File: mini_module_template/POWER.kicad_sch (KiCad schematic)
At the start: 15 parts, among them J2 PASS THROUYH BUS CONENCTOR, J4 PASS THROUYH BUS CONENCTOR, U5 AZ1117-3.3

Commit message: Leyout rev 1
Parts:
- removed C20: 10u, Capacitor_SMD:C_0805_2012Metric, symbol Device:C
- removed D6: HV_PWR, Diode_SMD:D_0603_1608Metric, symbol Device:LED
- removed J2, J4: PASS THROUYH BUS CONENCTOR, symbol Connector_Generic:Conn_01x07
- added C25, C26: 10u, Capacitor_SMD:C_1206_3216Metric, symbol Device:C
- added C28, C29: 22u, Capacitor_SMD:C_1206_3216Metric, symbol Device:C
- added C30: 100n, Capacitor_SMD:C_0603_1608Metric, symbol Device:C
- added C31: 1n, Capacitor_SMD:C_0603_1608Metric, symbol Device:C
- added C32: 100n, Capacitor_SMD:C_0402_1005Metric, symbol Device:C
- added J2, J3: ~, parts:DSUB-7w2, symbol DSUB_7w2:DSUB-7w2
- added L1: 3.3u, Inductor_SMD:L_Changjiang_FNR4030S, symbol Device:L
- added R25: 54k9, Resistor_SMD:R_0402_1005Metric, symbol Device:R
- added R26: 10k, Resistor_SMD:R_0402_1005Metric, symbol Device:R
- added U5: TPS563200, Package_TO_SOT_SMD:SOT-23-6, symbol Regulator_Switching:TPS563200
- C20: renamed from C15; footprint Capacitor_SMD:C_1206_3216Metric -> Capacitor_SMD:C_0805_2012Metric
- renumbered C16 to C21, C17 to C22, C18 to C23, C19 to C24, R22 to R27, R25 to R29, R23 to R30, U5 to U4
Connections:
- net +12V: now also C25.1, C26.1, J2.2 (D11), J3.2 (D11), U5.3 (VIN)
- net +5V: now also C28.1, C29.1, C30.1, C31.1, C32.1, L1.2, R25.1
- net CAN_H: now also J2.3 (D12), J3.3 (D12)
- net CAN_L: now also J2.4 (D13), J3.4 (D13)
- net GND: now also R24.2, C25.2, C26.2, C28.2, C29.2, C30.2, C31.2, J2.5 (D21), J2.7 (H2), J3.5 (D21), J3.7 (H2), R26.2, U5.1 (GND)
- net VCC: now also J2.1 (H1), J3.1 (H1); no longer R24.1
- new net: C32.2, U5.6 (VBST)
- new net: L1.1, U5.2 (SW)
- new net: R24.1, U5.5 (EN)
- new net: R25.2, R26.1, U5.4 (VFB)
- new net NC: J2.6 (D22), J3.6 (D22)
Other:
- note added: "DC-DC 12V TO 5V"
- note added: "Vout= 0.768(1+R1/R2) Vout=5V R1=54k9 R2=10k Vout=>4.984V"
- note removed: "SOME 12V TO 5V"

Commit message: a
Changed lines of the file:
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@@
-	)
-	(junction
-		(at 212.09 39.37)
-		(diameter 0)
-		(color 0 0 0 0)
 	)
 	(junction
@@
 		)
 		(stroke
-			(width 0)
-			(type default)
-		)
-	)
-	(wire
-		(pts
-			(xy 212.09 39.37) (xy 212.09 40.64)
-		)
-		(stroke

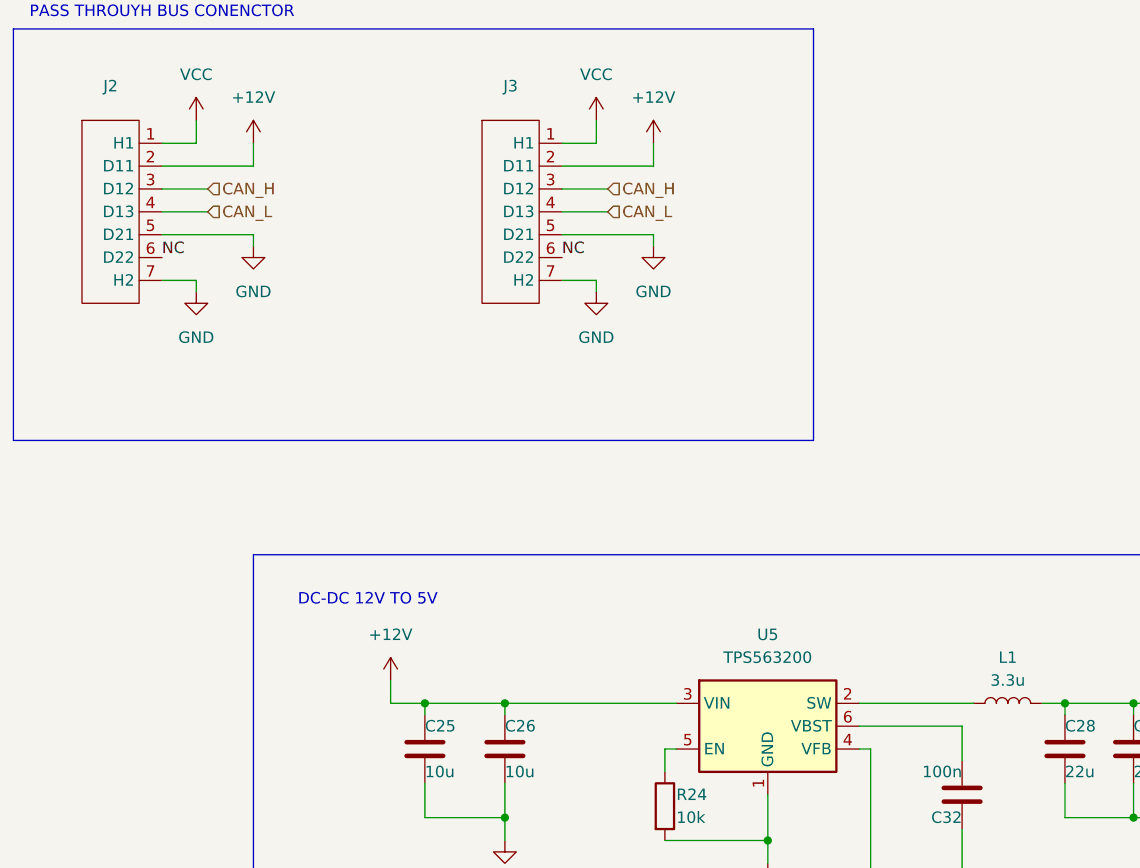
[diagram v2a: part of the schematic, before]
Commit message: fixed can and usb traces
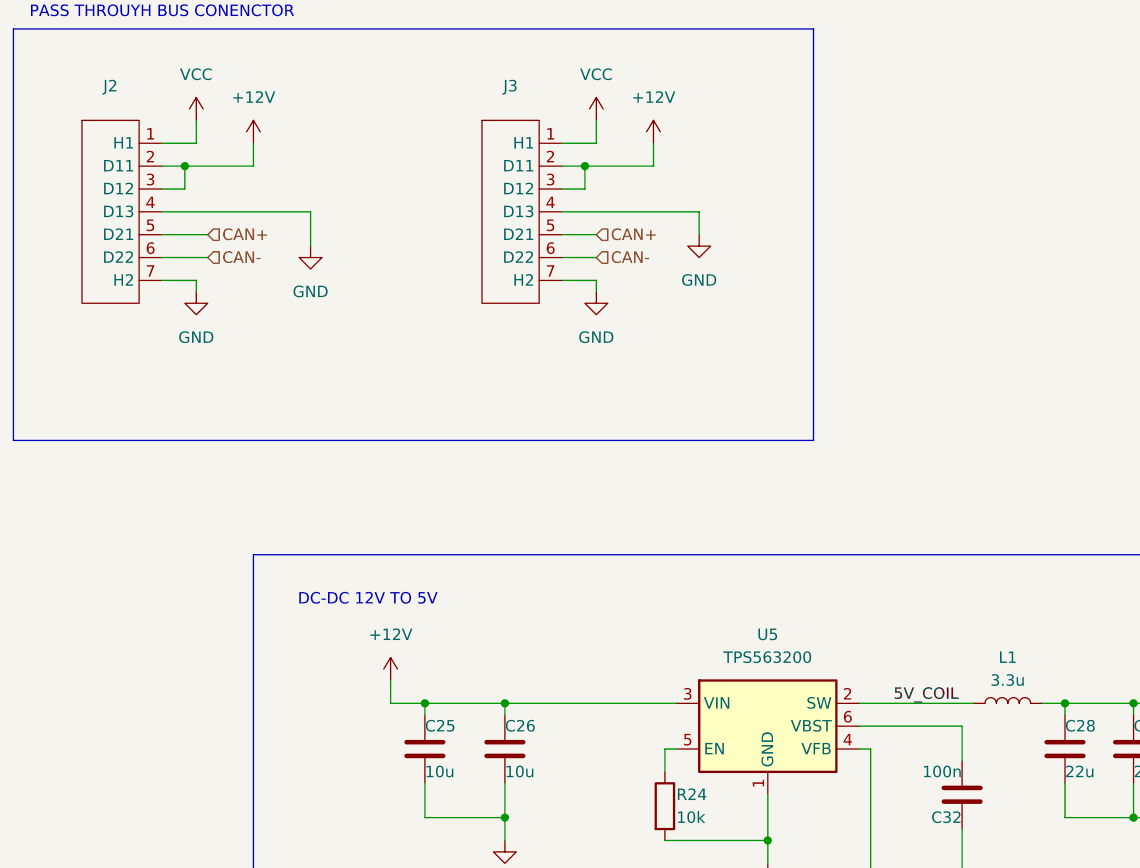
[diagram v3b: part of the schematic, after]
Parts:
- C25, C26, C28, C29: footprint Capacitor_SMD:C_1206_3216Metric -> Capacitor_SMD:C_0805_2012Metric
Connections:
- net CAN_H is gone; now on net +12V: J2.3 (D12), J3.3 (D12)
- net CAN_L is gone; now on net GND: J2.4 (D13), J3.4 (D13)
- net GND: no longer J2.5 (D21), J3.5 (D21)
- net 5V_COIL: now reaches L1.1, U5.2 (SW)
- net NC renamed CAN-
- new net CAN+: J2.5 (D21), J3.5 (D21)
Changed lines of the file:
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@@
 	)
 	(junction
+		(at 87.63 34.29)
+		(diameter 0)
+		(color 0 0 0 0)
+	)
+	(junction
 		(at 140.97 93.98)
 		(diameter 0)
@@
 	)
 	(junction
+		(at 43.18 34.29)
+		(diameter 0)
+		(color 0 0 0 0)
+	)
+	(junction
 		(at 171.45 93.98)
 		(diameter 0)
@@
 	(wire
 		(pts
-			(xy 50.8 41.91) (xy 40.64 41.91)
+			(xy 107.95 104.14) (xy 107.95 109.22)
 		)
 		(stroke
@@
 	(wire
 		(pts
-			(xy 107.95 104.14) (xy 107.95 109.22)
+			(xy 57.15 43.18) (xy 57.15 39.37)
 		)
 		(stroke
@@
 	(wire
 		(pts
+			(xy 87.63 34.29) (xy 95.25 34.29)
+		)
+		(stroke
+			(width 0)
+			(type default)
+		)
+	)
+	(wire
+		(pts
+			(xy 40.64 39.37) (xy 57.15 39.37)
+		)
+		(stroke
+			(width 0)
+			(type default)
+		)
+	)
+	(wire
+		(pts
 			(xy 44.45 29.21) (xy 44.45 31.75)
 		)
@@
 	(wire
 		(pts
+			(xy 85.09 41.91) (xy 88.9 41.91)
+		)
+		(stroke
+			(width 0)
+			(type default)
+		)
+	)
+	(wire
+		(pts
 			(xy 129.54 107.95) (xy 129.54 113.03)
 		)
@@
 	(wire
 		(pts
-			(xy 95.25 41.91) (xy 85.09 41.91)
-		)
-		(stroke
-			(width 0)
-			(type default)
-		)
-	)
-	(wire
-		(pts
 			(xy 189.23 59.69) (xy 196.85 59.69)
 		)
@@
 	(wire
 		(pts
+			(xy 100.33 39.37) (xy 85.09 39.37)
+		)
+		(stroke
+			(width 0)
+			(type default)
+		)
+	)
+	(wire
+		(pts
 			(xy 163.83 93.98) (xy 171.45 93.98)
 		)
@@
 	(wire
 		(pts
-			(xy 85.09 36.83) (xy 90.17 36.83)
+			(xy 85.09 36.83) (xy 87.63 36.83)
 		)
 		(stroke
@@
 	(wire
 		(pts
+			(xy 40.64 36.83) (xy 43.18 36.83)
+		)
+		(stroke
+			(width 0)
+			(type default)
+		)
+	)
+	(wire
+		(pts
 			(xy 176.53 93.98) (xy 176.53 104.14)
 		)
@@
 	(wire
 		(pts
+			(xy 40.64 44.45) (xy 45.72 44.45)
+		)
+		(stroke
+			(width 0)
+			(type default)
+		)
+	)
+	(wire
+		(pts
 			(xy 129.54 100.33) (xy 129.54 96.52)
 		)
@@
 	(wire
 		(pts
-			(xy 204.47 48.26) (xy 204.47 59.69)
+			(xy 40.64 41.91) (xy 45.72 41.91)
 		)
 		(stroke
@@
 	(wire
 		(pts
-			(xy 40.64 39.37) (xy 45.72 39.37)
+			(xy 85.09 44.45) (xy 88.9 44.45)
 		)
 		(stroke
@@
 	(wire
 		(pts
-			(xy 95.25 43.18) (xy 95.25 41.91)
+			(xy 204.47 48.26) (xy 204.47 59.69)
+		)
+		(stroke
+			(width 0)
+			(type default)
+		)
+	)
+	(wire
+		(pts
+			(xy 87.63 34.29) (xy 87.63 36.83)
 		)
 		(stroke
@@
 	(wire
 		(pts
-			(xy 50.8 43.18) (xy 50.8 41.91)
+			(xy 43.18 34.29) (xy 43.18 36.83)
 		)
 		(stroke
@@
 	(wire
 		(pts
-			(xy 50.8 34.29) (xy 40.64 34.29)
+			(xy 50.8 34.29) (xy 43.18 34.29)
 		)
 		(stroke
@@
 	(wire
 		(pts
+			(xy 87.63 34.29) (xy 85.09 34.29)
+		)
+		(stroke
+			(width 0)
+			(type default)
+		)
+	)
+	(wire
+		(pts
 			(xy 41.91 170.18) (xy 41.91 171.45)
 		)
@@
 	(wire
 		(pts
-			(xy 85.09 39.37) (xy 90.17 39.37)
+			(xy 189.23 39.37) (xy 196.85 39.37)
 		)
 		(stroke
@@
 	(wire
 		(pts
-			(xy 189.23 39.37) (xy 196.85 39.37)
+			(xy 100.33 41.91) (xy 100.33 39.37)
 		)
 		(stroke
@@
 	(wire
 		(pts
-			(xy 95.25 34.29) (xy 85.09 34.29)
+			(xy 43.18 34.29) (xy 40.64 34.29)
 		)
 		(stroke
@@
 	(wire
 		(pts
-			(xy 40.64 36.83) (xy 45.72 36.83)
-		)
-		(stroke
-			(width 0)
-			(type default)
-		)
-	)
-	(wire
-		(pts
 			(xy 160.02 39.37) (xy 160.02 40.64)
 		)
@@
 		)
 	)
-	(label "NC"
-		(at 40.64 44.45 0)
-		(fields_autoplaced yes)
-		(effects
-			(font
-				(size 1.27 1.27)
-			)
-			(justify left bottom)
-		)
-	)
-	(label "NC"
-		(at 85.09 44.45 0)
+	(label "5V_COIL"
+		(at 121.92 93.98 0)
 		(fields_autoplaced yes)
 		(effects
@@
 		)
 	)
-	(hierarchical_label "CAN_L"
+	(hierarchical_label "CAN-"
 		(shape input)
-		(at 45.72 39.37 0)
+		(at 45.72 44.45 0)
 		(fields_autoplaced yes)
 		(effects
@@
 		)
 	)
-	(hierarchical_label "CAN_L"
+	(hierarchical_label "CAN-"
 		(shape input)
-		(at 90.17 39.37 0)
+		(at 88.9 44.45 0)
 		(fields_autoplaced yes)
 		(effects
@@
 		)
 	)
-	(hierarchical_label "CAN_H"
+	(hierarchical_label "CAN+"
 		(shape input)
-		(at 90.17 36.83 0)
+		(at 88.9 41.91 0)
 		(fields_autoplaced yes)
 		(effects
@@
 		)
 	)
-	(hierarchical_label "CAN_H"
-		(shape input)
-		(at 45.72 36.83 0)
+	(hierarchical_label "V_SENSE"
+		(shape output)
+		(at 44.45 170.18 0)
 		(fields_autoplaced yes)
 		(effects
@@
 		)
 	)
-	(hierarchical_label "V_SENSE"
-		(shape output)
-		(at 44.45 170.18 0)
+	(hierarchical_label "CAN+"
+		(shape input)
+		(at 45.72 41.91 0)
 		(fields_autoplaced yes)
 		(effects
@@
 			)
 		)
-		(property "Footprint" "Capacitor_SMD:C_1206_3216Metric"
+		(property "Footprint" "Capacitor_SMD:C_0805_2012Metric"
 			(at 149.5552 102.87 0)
 			(effects
@@
 			)
 		)
-		(property "Footprint" "Capacitor_SMD:C_1206_3216Metric"
+		(property "Footprint" "Capacitor_SMD:C_0805_2012Metric"
 			(at 141.9352 102.87 0)
 			(effects
@@
 	(symbol
 		(lib_id "power:GND")
-		(at 95.25 43.18 0)
+		(at 100.33 41.91 0)
 		(unit 1)
 		(exclude_from_sim no)
@@
 		(fields_autoplaced yes)
 		(property "Reference" "#PWR050"
-			(at 95.25 49.53 0)
+			(at 100.33 48.26 0)
 			(effects
 				(font
@@
 		)
 		(property "Value" "GND"
-			(at 95.25 48.26 0)
+			(at 100.33 46.99 0)
 			(effects
 				(font
@@
 		)
 		(property "Footprint" ""
-			(at 95.25 43.18 0)
+			(at 100.33 41.91 0)
 			(effects
 				(font
@@
 		)
 		(property "Datasheet" ""
-			(at 95.25 43.18 0)
+			(at 100.33 41.91 0)
 			(effects
 				(font
@@
 		)
 		(property "Description" "Power symbol creates a global label with name \"GND\" , ground"
-			(at 95.25 43.18 0)
+			(at 100.33 41.91 0)
 			(effects
 				(font
@@
 			)
 		)
-		(property "Footprint" "Capacitor_SMD:C_1206_3216Metric"
+		(property "Footprint" "Capacitor_SMD:C_0805_2012Metric"
 			(at 79.7052 102.87 0)
 			(effects
@@
 	(symbol
 		(lib_id "power:GND")
-		(at 50.8 43.18 0)
+		(at 57.15 43.18 0)
 		(unit 1)
 		(exclude_from_sim no)
@@
 		(fields_autoplaced yes)
 		(property "Reference" "#PWR049"
-			(at 50.8 49.53 0)
+			(at 57.15 49.53 0)
 			(effects
 				(font
@@
 		)
 		(property "Value" "GND"
-			(at 50.8 48.26 0)
+			(at 57.15 48.26 0)
 			(effects
 				(font
@@
 		)
 		(property "Footprint" ""
-			(at 50.8 43.18 0)
+			(at 57.15 43.18 0)
 			(effects
 				(font
@@
 		)
 		(property "Datasheet" ""
-			(at 50.8 43.18 0)
+			(at 57.15 43.18 0)
 			(effects
 				(font
@@
 		)
 		(property "Description" "Power symbol creates a global label with name \"GND\" , ground"
-			(at 50.8 43.18 0)
+			(at 57.15 43.18 0)
 			(effects
 				(font
@@
 			)
 		)
-		(property "Footprint" "Capacitor_SMD:C_1206_3216Metric"
+		(property "Footprint" "Capacitor_SMD:C_0805_2012Metric"
 			(at 70.8152 102.87 0)
 			(effects

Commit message: rev 1.0 finished
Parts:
- added Q2: AO3400A, Package_TO_SOT_SMD:SOT-23, symbol Transistor_FET:AO3400A
- added R28: 1k, Resistor_SMD:R_0402_1005Metric, symbol Device:R
- added R44: 100k, Resistor_SMD:R_0402_1005Metric, symbol Device:R
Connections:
- net +12V: now also R28.1; no longer J2.3 (D12), J3.3 (D12)
- net +5V: now also Q2.3 (D); no longer C28.1, C29.1, C30.1, C31.1, C32.1, L1.2, R25.1
- net 5V_COIL: now also C32.1
- net GND: now also R44.2; no longer J2.4 (D13), J3.4 (D13)
- new net: Q2.1 (G), R28.2, R44.1
- new net 5V_mosfet: C28.1, C29.1, C30.1, C31.1, L1.2, Q2.2 (S), R25.1
- new net USB_DOWNSTREAM_D+: J3.3 (D12)
- new net USB_DOWNSTREAM_D-: J3.4 (D13)
- new net USB_UPSTREAM_D+: J2.3 (D12)
- new net USB_UPSTREAM_D-: J2.4 (D13)
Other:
- moved on the sheet: C32
